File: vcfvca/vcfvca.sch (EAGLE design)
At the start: 104 parts, among them IC1 LM13700N, IC2 LM4558N, IC3 LM13700N, IC4 LM13700N, IC5 LM4558N, J1 POWER, J2 FREQ, J3 RES, J4 AMP, J5 AUD_IN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

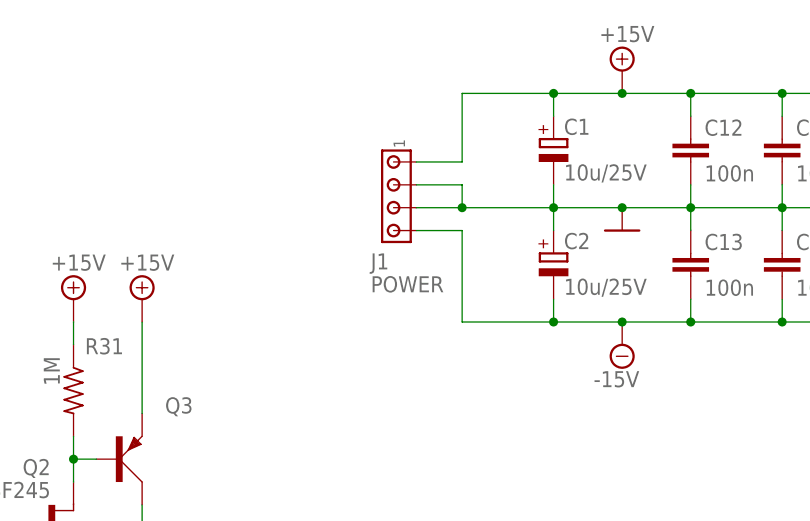
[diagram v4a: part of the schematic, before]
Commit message: Add ferrite bead, reroute
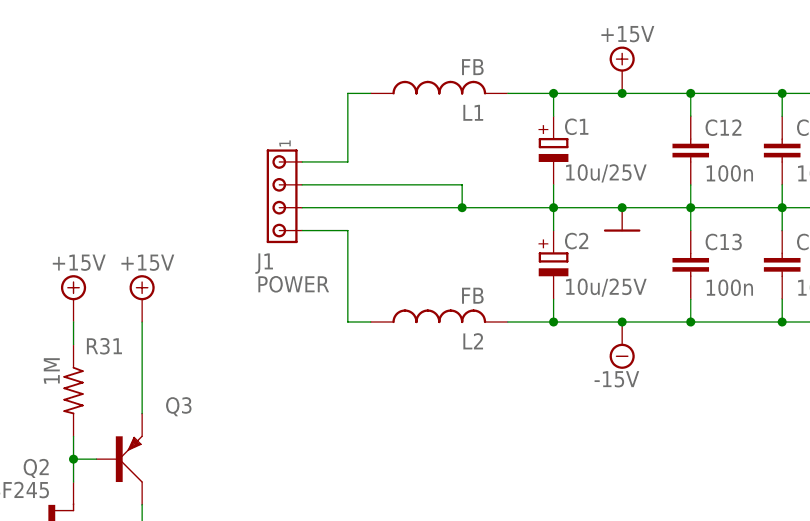
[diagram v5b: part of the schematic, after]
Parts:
- added L1, L2: FB, rcl:L-US0207/10
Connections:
- new net N$63: J1.1, L1.1
- new net N$64: J1.4, L2.1
- net +15V: now also L1.2; no longer J1.1
- net -15V: now also L2.2; no longer J1.4
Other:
- moved on the sheet: J1
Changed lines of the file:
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@@
 <part name="J6" library="pinhead" library_urn="urn:adsk.eagle:library:325" deviceset="PINHD-1X2" device="" package3d_urn="urn:adsk.eagle:package:22435/2" value="AUD_OUT"/>
 <part name="GND35" library="supply1" library_urn="urn:adsk.eagle:library:371" deviceset="GND" device=""/>
+<part name="L1" library="rcl" library_urn="urn:adsk.eagle:library:334" deviceset="L-US" device="0207/10" package3d_urn="urn:adsk.eagle:package:23491/2" value="FB"/>
+<part name="L2" library="rcl" library_urn="urn:adsk.eagle:library:334" deviceset="L-US" device="0207/10" package3d_urn="urn:adsk.eagle:package:23491/2" value="FB"/>
 </parts>
 <sheets>
@@
 </plain>
 <instances>
-<instance part="J1" gate="G$3" x="246.38" y="241.3" smashed="yes" rot="MR270">
-<attribute name="NAME" x="243.84" y="231.14" size="1.778" layer="95" rot="MR180"/>
-<attribute name="VALUE" x="243.84" y="228.6" size="1.778" layer="96" rot="MR180"/>
+<instance part="J1" gate="G$3" x="233.68" y="241.3" smashed="yes" rot="MR270">
+<attribute name="NAME" x="231.14" y="231.14" size="1.778" layer="95" rot="MR180"/>
+<attribute name="VALUE" x="231.14" y="228.6" size="1.778" layer="96" rot="MR180"/>
 </instance>
 <instance part="SUPPLY1" gate="+15V" x="271.78" y="251.46" smashed="yes">
@@
 </instance>
 <instance part="GND35" gate="1" x="350.52" y="172.72" smashed="yes"/>
+<instance part="L1" gate="G$1" x="251.46" y="248.92" smashed="yes" rot="R90">
+<attribute name="NAME" x="256.54" y="247.65" size="1.778" layer="95" rot="R180"/>
+<attribute name="VALUE" x="256.54" y="252.73" size="1.778" layer="96" rot="R180"/>
+</instance>
+<instance part="L2" gate="G$1" x="251.46" y="223.52" smashed="yes" rot="R90">
+<attribute name="NAME" x="256.54" y="222.25" size="1.778" layer="95" rot="R180"/>
+<attribute name="VALUE" x="256.54" y="227.33" size="1.778" layer="96" rot="R180"/>
+</instance>
 </instances>
 <busses>
@@
 <wire x1="279.4" y1="246.38" x2="279.4" y2="248.92" width="0.1524" layer="91"/>
 <junction x="279.4" y="248.92"/>
-<wire x1="254" y1="241.3" x2="254" y2="248.92" width="0.1524" layer="91"/>
-<pinref part="J1" gate="G$3" pin="1"/>
-<wire x1="248.92" y1="241.3" x2="254" y2="241.3" width="0.1524" layer="91"/>
 <pinref part="C1" gate="G$1" pin="+"/>
 <wire x1="264.16" y1="246.38" x2="264.16" y2="248.92" width="0.1524" layer="91"/>
-<wire x1="254" y1="248.92" x2="264.16" y2="248.92" width="0.1524" layer="91"/>
 <wire x1="264.16" y1="248.92" x2="271.78" y2="248.92" width="0.1524" layer="91"/>
+<junction x="271.78" y="248.92"/>
+<pinref part="L1" gate="G$1" pin="2"/>
+<wire x1="259.08" y1="248.92" x2="264.16" y2="248.92" width="0.1524" layer="91"/>
 <junction x="264.16" y="248.92"/>
-<junction x="271.78" y="248.92"/>
 </segment>
 <segment>
@@
 <pinref part="J1" gate="G$3" pin="2"/>
 <wire x1="264.16" y1="236.22" x2="254" y2="236.22" width="0.1524" layer="91"/>
-<wire x1="254" y1="236.22" x2="248.92" y2="236.22" width="0.1524" layer="91"/>
-<wire x1="248.92" y1="238.76" x2="254" y2="238.76" width="0.1524" layer="91"/>
+<wire x1="254" y1="236.22" x2="236.22" y2="236.22" width="0.1524" layer="91"/>
+<wire x1="236.22" y1="238.76" x2="254" y2="238.76" width="0.1524" layer="91"/>
 <wire x1="254" y1="238.76" x2="254" y2="236.22" width="0.1524" layer="91"/>
 <junction x="254" y="236.22"/>
@@
 <net name="-15V" class="0">
 <segment>
-<pinref part="J1" gate="G$3" pin="4"/>
-<wire x1="248.92" y1="233.68" x2="254" y2="233.68" width="0.1524" layer="91"/>
-<wire x1="254" y1="233.68" x2="254" y2="223.52" width="0.1524" layer="91"/>
 <pinref part="SUPPLY2" gate="G$1" pin="-15V"/>
-<wire x1="254" y1="223.52" x2="264.16" y2="223.52" width="0.1524" layer="91"/>
 <pinref part="C2" gate="G$1" pin="-"/>
 <wire x1="264.16" y1="223.52" x2="271.78" y2="223.52" width="0.1524" layer="91"/>
 <wire x1="264.16" y1="226.06" x2="264.16" y2="223.52" width="0.1524" layer="91"/>
-<junction x="264.16" y="223.52"/>
 <pinref part="IC5" gate="P" pin="V-"/>
 <wire x1="271.78" y1="223.52" x2="279.4" y2="223.52" width="0.1524" layer="91"/>
@@
 <wire x1="279.4" y1="226.06" x2="279.4" y2="223.52" width="0.1524" layer="91"/>
 <junction x="279.4" y="223.52"/>
+<pinref part="L2" gate="G$1" pin="2"/>
+<wire x1="259.08" y1="223.52" x2="264.16" y2="223.52" width="0.1524" layer="91"/>
+<junction x="264.16" y="223.52"/>
 </segment>
 <segment>
@@
 </segment>
 </net>
+<net name="N$63" class="0">
+<segment>
+<pinref part="L1" gate="G$1" pin="1"/>
+<wire x1="243.84" y1="248.92" x2="241.3" y2="248.92" width="0.1524" layer="91"/>
+<wire x1="241.3" y1="248.92" x2="241.3" y2="241.3" width="0.1524" layer="91"/>
+<pinref part="J1" gate="G$3" pin="1"/>
+<wire x1="241.3" y1="241.3" x2="236.22" y2="241.3" width="0.1524" layer="91"/>
+</segment>
+</net>
+<net name="N$64" class="0">
+<segment>
+<pinref part="J1" gate="G$3" pin="4"/>
+<wire x1="236.22" y1="233.68" x2="241.3" y2="233.68" width="0.1524" layer="91"/>
+<wire x1="241.3" y1="233.68" x2="241.3" y2="223.52" width="0.1524" layer="91"/>
+<pinref part="L2" gate="G$1" pin="1"/>
+<wire x1="241.3" y1="223.52" x2="243.84" y2="223.52" width="0.1524" layer="91"/>
+</segment>
+</net>

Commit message: Export images
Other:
- note added: "Kenobi (based on OB-1) 4-pole VCF/VCA Tuwuh S Wibowo ACMS Spring 2020 Apr '20"
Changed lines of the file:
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@@
 <text x="284.48" y="198.12" size="1.778" layer="91">VCA</text>
 <text x="266.7" y="124.46" size="1.778" layer="91">Resonance feedback</text>
+<text x="172.72" y="233.68" size="1.778" layer="91">Kenobi (based on OB-1)
+4-pole VCF/VCA
+Tuwuh S Wibowo
+ACMS Spring 2020
+Apr '20</text>
 </plain>
 <instances>

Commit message: VCF/VCA: revision for final submission
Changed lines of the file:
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@@
 <instance part="Q3" gate="1" x="215.9" y="208.28" smashed="yes">
 <attribute name="NAME" x="220.98" y="213.36" size="1.778" layer="95"/>
-<attribute name="VALUE" x="220.98" y="195.58" size="1.778" layer="96"/>
+<attribute name="VALUE" x="220.98" y="210.82" size="1.778" layer="96"/>
 </instance>
 <instance part="IC2" gate="B" x="320.04" y="180.34" smashed="yes" rot="MR180">
